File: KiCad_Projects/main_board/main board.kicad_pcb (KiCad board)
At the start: 2 copper layers, 77 parts, among them J1 Conn_01x04_Female, J2 Conn_01x04_Female, J3 Conn_01x02_Female, J4 Conn_01x05_Female, SW1 SW_Push, SW2 SW_Push, U1 open_mv, U10 Seeeduino_Xiao, U11 Seeeduino_Xiao, U12 TSSP58038, U13 TSSP58038, U14 TSSP58038, U15 TSSP58038, U2 type-c_sirial, U3 PIC18F26K20_ISS, U4 Akizuki_Logiv_Level_converter, U5 MPU6050, U6 TSSP58038, U7 TSSP58038, U8 TSSP58038, U9 TSSP58038

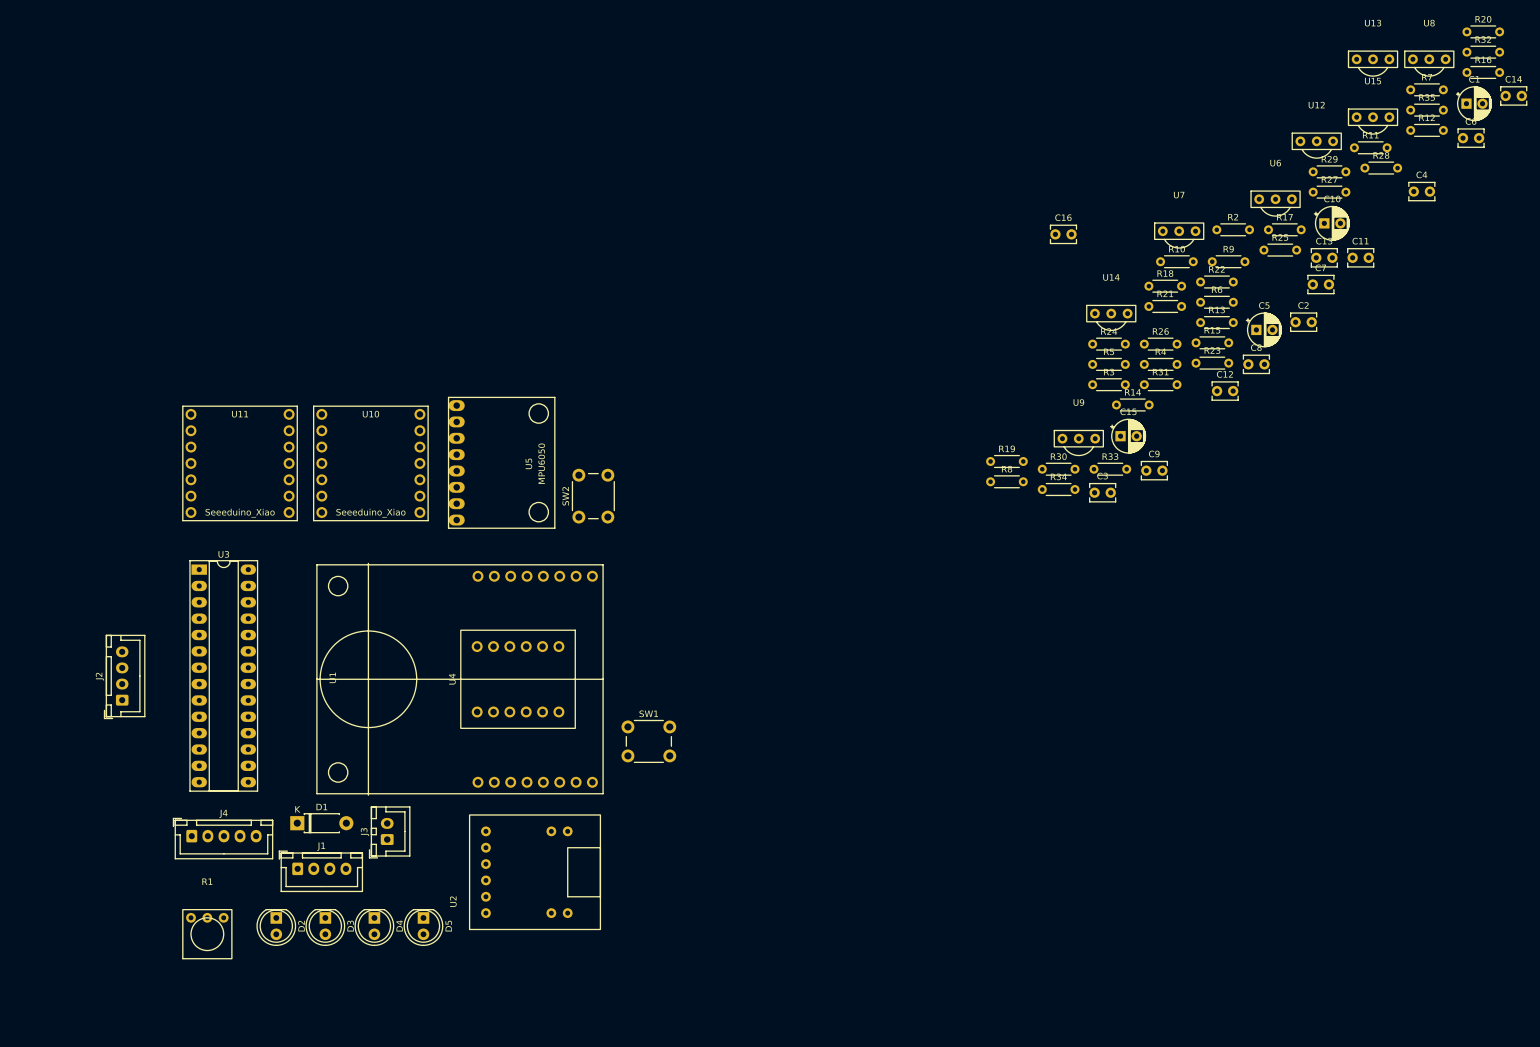
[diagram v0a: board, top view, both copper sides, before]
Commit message: 基板データの更新
メイン基板の部品配置まででけた
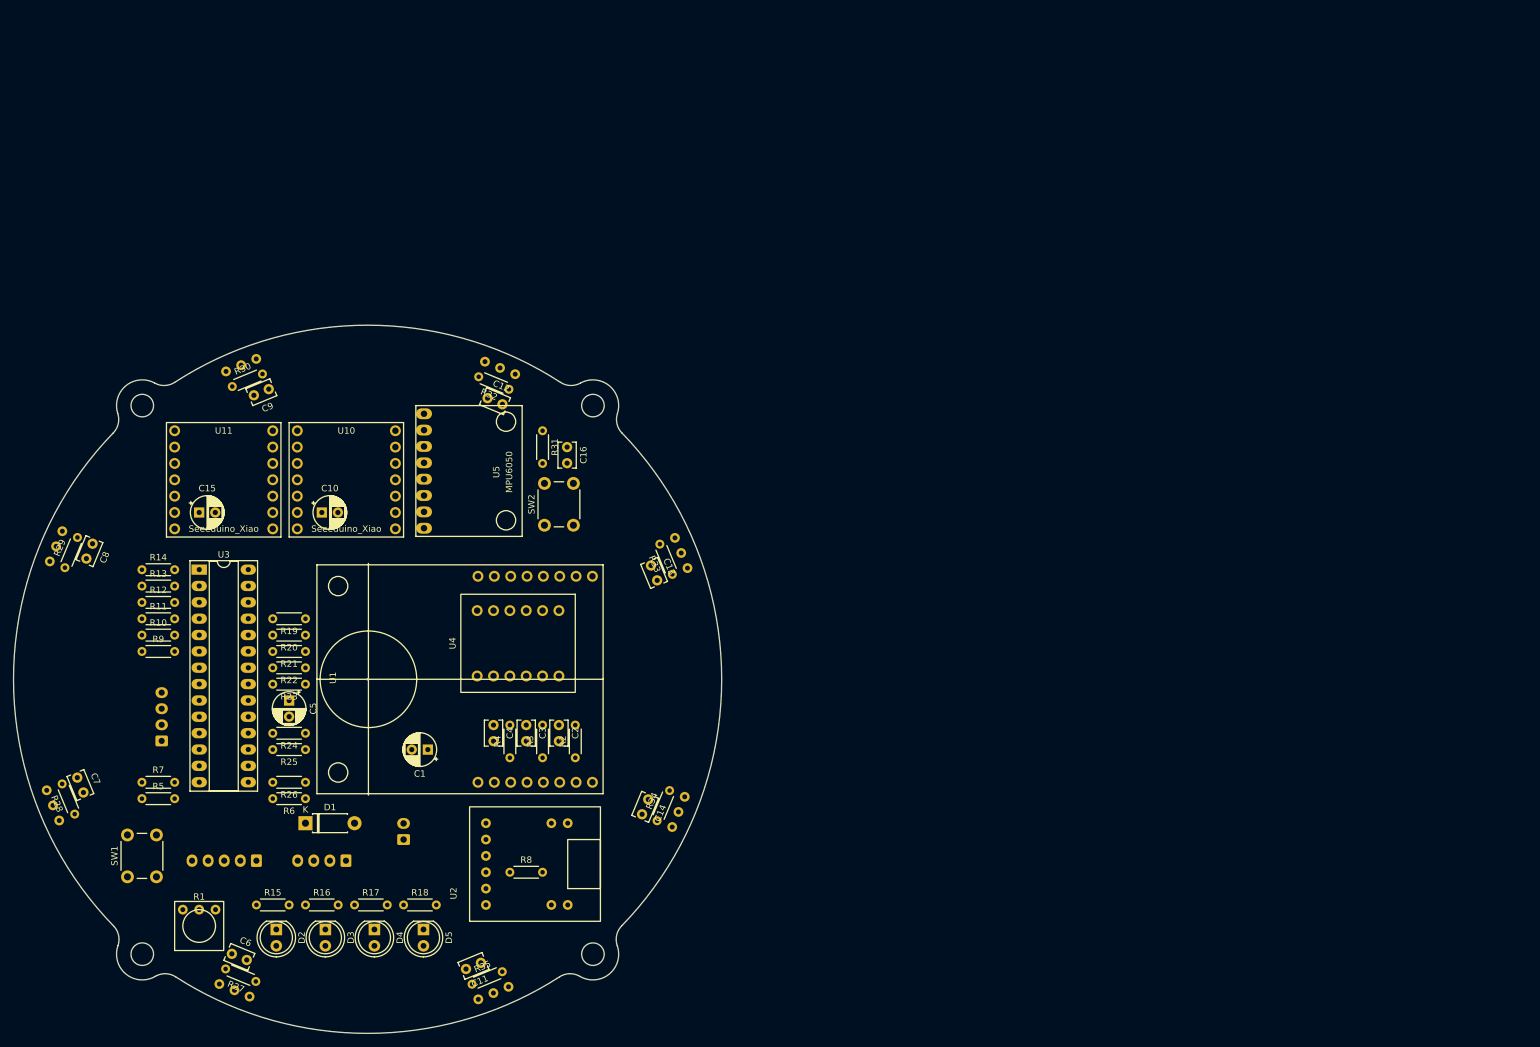
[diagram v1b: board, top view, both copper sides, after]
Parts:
- J1, J2, J3, J4, U12, U13, U14, U15, U6, U7, U8, U9: moved to B.Cu
- moved C6 229.4 mm to (80.0, 160.0), turned to -22.5 degrees
- moved R7 224.5 mm to (66.0, 133.3)
- moved U8 224.4 mm to (57.4, 98.6), turned to 67.5 degrees
- moved R28 224.1 mm to (55.6, 138.3), turned to 112.5 degrees
- moved R16 222.0 mm to (91.4, 152.4)
- moved R12 210.3 mm to (66.0, 105.4)
- moved C7 206.6 mm to (56.0, 132.6), turned to -67.5 degrees
- moved R27 205.0 mm to (83.7, 164.3), turned to 157.5 degrees
- moved R29 203.4 mm to (54.1, 100.0), turned to 67.5 degrees
- moved R20 203.3 mm to (91.4, 110.5), turned to 180 degrees
- moved R11 202.0 mm to (66.0, 108.0)
- moved U6 201.8 mm to (82.4, 161.0), turned to 157.5 degrees
- moved R35 199.2 mm to (117.3, 164.7), turned to 22.5 degrees
- moved U15 194.5 mm to (118.7, 161.4), turned to -157.5 degrees
- moved U7 193.7 mm to (56.9, 135.0), turned to 112.5 degrees
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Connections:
- C11 pad 2: RES -> +3V3
- C12 pad 2: RES -> +3V3
- C13 pad 2: RES -> +3V3
- C14 pad 2: RES -> +3V3
- R32 pad 1: RES -> +3V3
- R33 pad 1: RES -> +3V3
- R34 pad 1: RES -> +3V3
- R35 pad 1: RES -> +3V3
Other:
- board outline added: 110 x 110 mm

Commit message: 基板データの更新
最後に更新してからのデータ全てです。
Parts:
- moved C11 88.5 mm to (117.7, 72.9), turned to -22.5 degrees
- moved R8 70.8 mm to (58.9, 117.6)
- moved R2 47.5 mm to (111.5, 87.4), turned to 180 degrees
- moved C2 42.3 mm to (106.4, 89.9), turned to 0 degrees
- moved R3 40.7 mm to (111.5, 92.5), turned to 180 degrees
- moved C3 35.2 mm to (106.4, 95.0), turned to 0 degrees
- moved C1 34.5 mm to (94.8, 97.5), turned to 0 degrees
- moved C12 34.3 mm to (144.3, 97.7), turned to -67.5 degrees
- moved C13 34.3 mm to (145.5, 134.0), turned to -111.5 degrees
- moved C14 34.2 mm to (120.9, 160.5), turned to -157.5 degrees
- moved R4 34.1 mm to (111.5, 97.5), turned to 180 degrees
- moved C16 34.0 mm to (147.6, 111.5)
- moved R31 34.0 mm to (143.8, 109.0)
- moved SW2 34.0 mm to (144.1, 123.6)
- moved C10 32.0 mm to (125.8, 94.5)
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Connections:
- C1 pad 2: RES -> GND
- C10 pad 2: RES -> GND
- C11 pad 1: RES -> IR1
- C11 pad 2: +3V3 -> GND
- C12 pad 1: RES -> IR2
- C12 pad 2: +3V3 -> GND
- C13 pad 1: RES -> IR3
- C13 pad 2: +3V3 -> GND
- C14 pad 1: RES -> IR4
- C14 pad 2: +3V3 -> GND
- C15 pad 2: RES -> GND
- C16 pad 1: Net-(C16-Pad1) -> RES
- C16 pad 2: RES -> GND
- C2 pad 2: RES -> GND
- C3 pad 2: RES -> GND
- C4 pad 2: RES -> GND
- C5 pad 2: RES -> GND
- C6 pad 1: +3V3 -> GND
- C6 pad 2: RES -> IR5
- C7 pad 1: +3V3 -> GND
- C7 pad 2: RES -> IR6
- C8 pad 1: +3V3 -> GND
- C8 pad 2: RES -> IR7
- C9 pad 1: +3V3 -> GND
- C9 pad 2: RES -> IR8
- D2 pad 1: RES -> GND
- D3 pad 1: RES -> GND
- D4 pad 1: RES -> GND
- D5 pad 1: RES -> GND
- J1 pad 1: RES -> GND
- J2 pad 3: RES -> GND
- J3 pad 1: RES -> GND
- J4 pad 1: RES -> GND
- R27 pad 1: Net-(R27-Pad1) -> Net-(U6-Pad0)
- R27 pad 2: +3V3 -> IR5
- R28 pad 1: Net-(R28-Pad1) -> Net-(U7-Pad0)
- R28 pad 2: +3V3 -> IR6
- R29 pad 1: Net-(R29-Pad1) -> Net-(U8-Pad0)
- R29 pad 2: +3V3 -> IR7
- R30 pad 1: Net-(R30-Pad1) -> Net-(U9-Pad0)
- R30 pad 2: +3V3 -> IR8
- R31 pad 2: Net-(C16-Pad1) -> RES
- R32 pad 1: +3V3 -> IR1
- R32 pad 2: Net-(R32-Pad2) -> Net-(U12-Pad0)
- R33 pad 1: +3V3 -> IR2
- R33 pad 2: Net-(R33-Pad2) -> Net-(U13-Pad0)
- R34 pad 1: +3V3 -> IR3
- R34 pad 2: Net-(R34-Pad2) -> Net-(U14-Pad0)
- R35 pad 1: +3V3 -> IR4
- R35 pad 2: Net-(R35-Pad2) -> Net-(U15-Pad0)
- SW1 pad 2: RES -> GND
- SW2 pad 1: Net-(C16-Pad1) -> RES
- SW2 pad 2: RES -> GND
- U1 pad 9: RES -> GND
- U10 pad 13: RES -> GND
- U11 pad 13: RES -> GND
- U12 pad 0: IR1 -> Net-(U12-Pad0)
- U12 pad 1: RES -> GND
- U12 pad 2: Net-(R32-Pad2) -> +3V3
- U13 pad 0: IR2 -> Net-(U13-Pad0)
- U13 pad 1: RES -> GND
- U13 pad 2: Net-(R33-Pad2) -> +3V3
- U14 pad 0: IR3 -> Net-(U14-Pad0)
- U14 pad 1: RES -> GND
- U14 pad 2: Net-(R34-Pad2) -> +3V3
- U15 pad 0: IR4 -> Net-(U15-Pad0)
- U15 pad 1: RES -> GND
- U15 pad 2: Net-(R35-Pad2) -> +3V3
- U2 pad 1: RES -> GND
- U3 pad 19: RES -> GND
- U3 pad 8: RES -> GND
- U4 pad 10: RES -> GND
- U4 pad 3: RES -> GND
- U5 pad 2: RES -> GND
- U6 pad 0: IR5 -> Net-(U6-Pad0)
- U6 pad 1: RES -> GND
- U6 pad 2: Net-(R27-Pad1) -> +3V3
- U7 pad 0: IR6 -> Net-(U7-Pad0)
- U7 pad 1: RES -> GND
- U7 pad 2: Net-(R28-Pad1) -> +3V3
- U8 pad 0: IR7 -> Net-(U8-Pad0)
- U8 pad 1: RES -> GND
- U8 pad 2: Net-(R29-Pad1) -> +3V3
- U9 pad 0: IR8 -> Net-(U9-Pad0)
- U9 pad 1: RES -> GND
- U9 pad 2: Net-(R30-Pad1) -> +3V3
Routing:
- net GND: track 0.00 -> 548.2 mm, vias 0 -> 3
- net +5V: track 0.00 -> 362.1 mm
- net +3V3: track 0.00 -> 351.3 mm, vias 0 -> 1
- net Net-(SW1-Pad1): track 0.00 -> 157.5 mm
- net IR4: track 0.00 -> 123.8 mm, vias 0 -> 10
- net SW2: track 0.00 -> 116.7 mm, vias 0 -> 5
- net IR3: track 0.00 -> 111.8 mm, vias 0 -> 4
- net Net-(J1-Pad4): track 0.00 -> 93.3 mm, vias 0 -> 4
- net IR2: track 0.00 -> 91.5 mm, vias 0 -> 1
- net IR5: track 0.00 -> 89.3 mm, vias 0 -> 3
- net AD2: track 0.00 -> 82.1 mm
- net AD1: track 0.00 -> 75.6 mm
- net PWR LED: track 0.00 -> 73.6 mm, vias 0 -> 1
- net AD5: track 0.00 -> 69.8 mm, vias 0 -> 3
- net IR6: track 0.00 -> 67.7 mm
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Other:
- outline, holes or cut-outs redrawn

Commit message: 基板データの更新
最新バージョンの発注データの作成
最新バージョンの発注。
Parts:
- Gyro Calibration: renamed from SW2
- OpenMV Reset: renamed from SW1
- U1 Open MV: renamed from U1
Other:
- board text added: "2022-2023 Munatyuu_Artemis Main Board Powered by TJ3B Designed by 抹茶"
- board text added: "Main Board Powered by TJ3B"
- board text added: "Munachu_Artemis"
